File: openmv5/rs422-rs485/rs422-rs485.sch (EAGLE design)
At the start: 90 parts, among them IC1 TPS613222ADBVR, IC2 AP64060WU-7, IC3 LM321LVIDCKR, IC4 74LVC1G07GW,125, IC5 THVD1426DR, IC6 THVD1426DR, J1 OPENMV5-TOP, J2 1771088, Q1 SSM3J356R,LF, U1 74LVC1G17SE-7, U2 74AHC1G08SE-7

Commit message: Fix wrong resistor value
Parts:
- R10, R12, R13, R14, R15: MPN CRCW04021K00FKEDC -> AC0402FR-1310KL
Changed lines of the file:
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@@
 </part>
 <part name="R10" library="sfe" deviceset="RESISTOR" device="0402-RES" value="10K">
-<attribute name="MPN" value="CRCW04021K00FKEDC"/>
+<attribute name="MPN" value="AC0402FR-1310KL"/>
 </part>
 <part name="GND5" library="sfe" deviceset="GND" device=""/>
@@
 </part>
 <part name="R12" library="sfe" deviceset="RESISTOR" device="0402-RES" value="10K">
-<attribute name="MPN" value="CRCW04021K00FKEDC"/>
+<attribute name="MPN" value="AC0402FR-1310KL"/>
 </part>
 <part name="R13" library="sfe" deviceset="RESISTOR" device="0402-RES" value="10K">
-<attribute name="MPN" value="CRCW04021K00FKEDC"/>
+<attribute name="MPN" value="AC0402FR-1310KL"/>
 </part>
 <part name="P+1" library="mux" deviceset="VCC" device=""/>
@@
 </part>
 <part name="R14" library="sfe" deviceset="RESISTOR" device="0402-RES" value="10K">
-<attribute name="MPN" value="CRCW04021K00FKEDC"/>
+<attribute name="MPN" value="AC0402FR-1310KL"/>
 </part>
 <part name="R15" library="sfe" deviceset="RESISTOR" device="0402-RES" value="10K">
-<attribute name="MPN" value="CRCW04021K00FKEDC"/>
+<attribute name="MPN" value="AC0402FR-1310KL"/>
 </part>
 <part name="R18" library="rcl" library_urn="urn:adsk.eagle:library:334" deviceset="R-US_" device="R0805" package3d_urn="urn:adsk.eagle:package:23553/2" value="10">

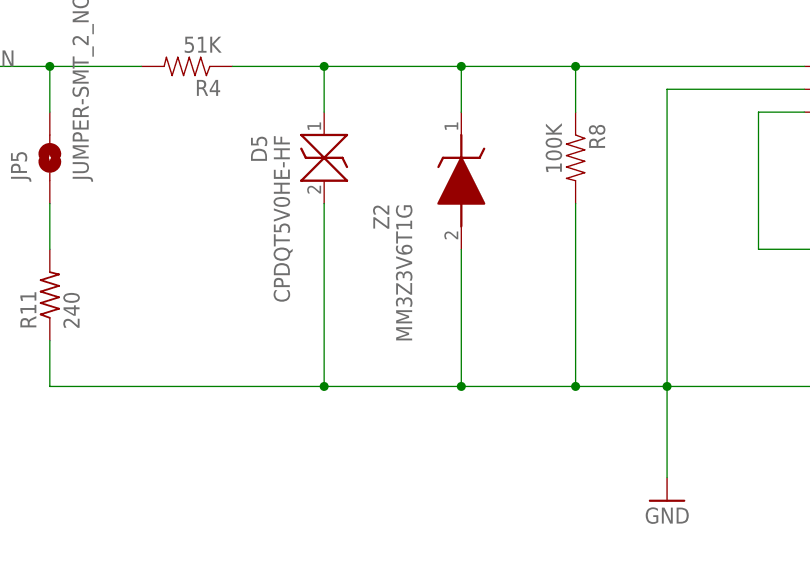
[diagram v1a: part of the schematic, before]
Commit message: Remove zener diode from ADC circuit
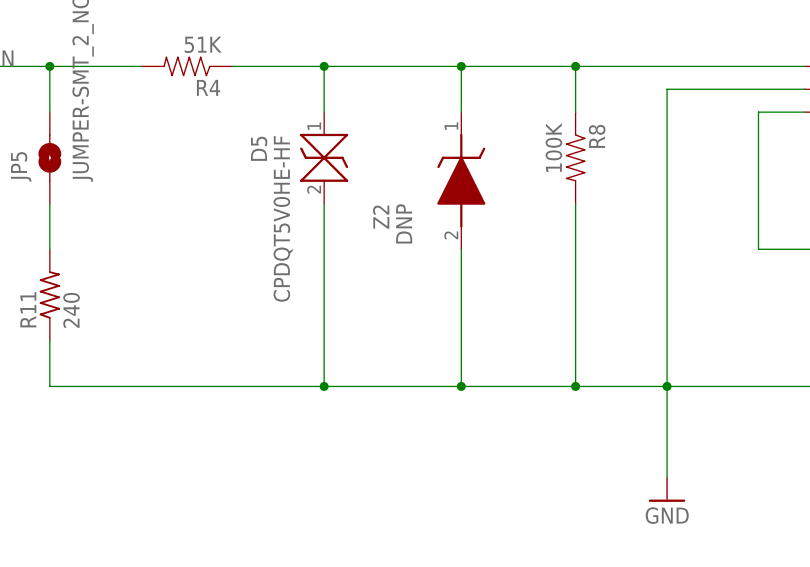
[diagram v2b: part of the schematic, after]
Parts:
- Z2: value MM3Z3V6T1G -> DNP; POPULATE (none) -> 0
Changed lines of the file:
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@@
 </part>
 <part name="GND7" library="sfe" deviceset="GND" device=""/>
-<part name="Z2" library="MM3Z3V6T1G" deviceset="MM3Z3V6T1G" device="">
+<part name="Z2" library="MM3Z3V6T1G" deviceset="MM3Z3V6T1G" device="" value="DNP">
 <attribute name="MPN" value="MM3Z3V6T1G"/>
+<attribute name="POPULATE" value="0"/>
 </part>
 <part name="R11" library="rcl" library_urn="urn:adsk.eagle:library:334" deviceset="R-US_" device="R0603" package3d_urn="urn:adsk.eagle:package:23555/3" value="240">
@@
 <attribute name="VALUE" x="308.61" y="233.68" size="1.778" layer="96" rot="MR270" align="center-left"/>
 <attribute name="MPN" x="314.96" y="243.84" size="1.778" layer="96" rot="MR270" display="off"/>
+<attribute name="POPULATE" x="314.96" y="243.84" size="1.778" layer="96" rot="MR270" display="off"/>
 </instance>
 <instance part="R11" gate="G$1" x="269.24" y="223.52" smashed="yes" rot="R90">
